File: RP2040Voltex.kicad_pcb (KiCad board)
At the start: 2 copper layers, 180 x 100 mm, 72 parts, among them J2 SWD_Connector, SW1 SW_Push_Dual_x2, SW2 K2-1102SP-C4SC-04, U1 RT8096C, U2 W25Q128JVS, U3 RP2040, U4 PEC16-4015F-N0024, U5 PEC16-4015F-N0024, Y1 Crystal_GND24

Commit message: Make capacitor closer to encoders
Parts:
- moved C18 19.3 mm to (58.8, 80.2), turned to 180 degrees
- moved C21 14.1 mm to (205.1, 80.2), turned to 0 degrees
- moved C20 12.1 mm to (65.3, 80.2), turned to 0 degrees
- moved C19 6.93 mm to (198.5, 80.2), turned to 180 degrees
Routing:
- net VBUS: track 386.8 -> 382.7 mm
- net /GPIO2: track 96.3 -> 99.0 mm
- net /GPIO29_ADC3: track 55.5 -> 58.1 mm
- net /GPIO28_ADC2: track 49.8 -> 52.4 mm
- net /GPIO3: track 90.2 -> 92.5 mm
- net GND: track 60.7 -> 58.8 mm, vias 43 -> 44

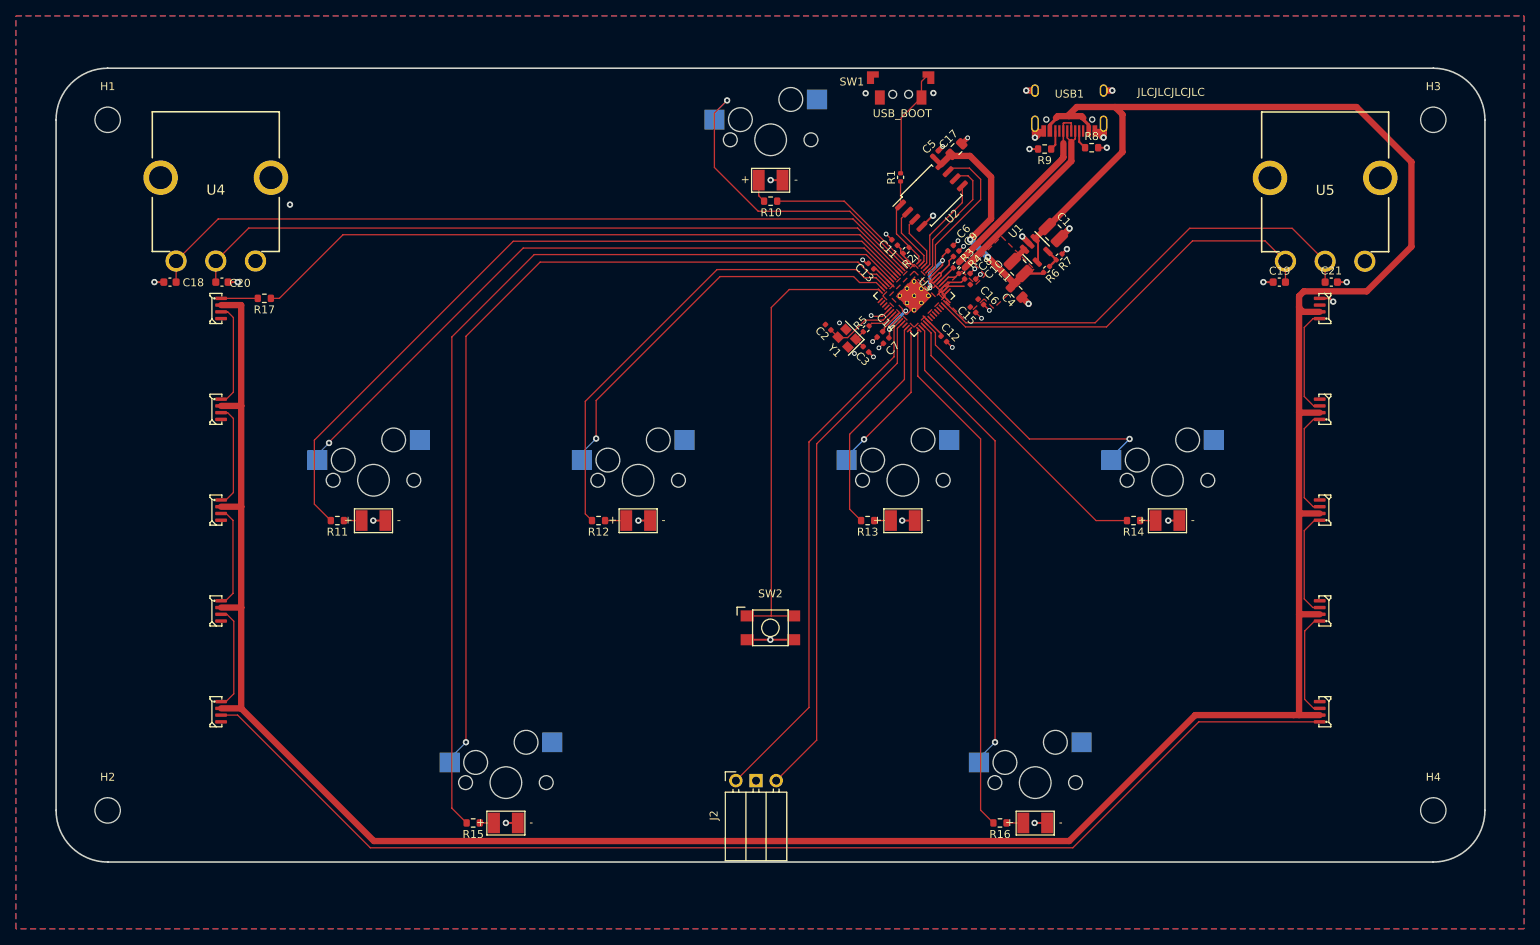
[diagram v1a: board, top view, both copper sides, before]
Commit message: Change front plane to be power plane
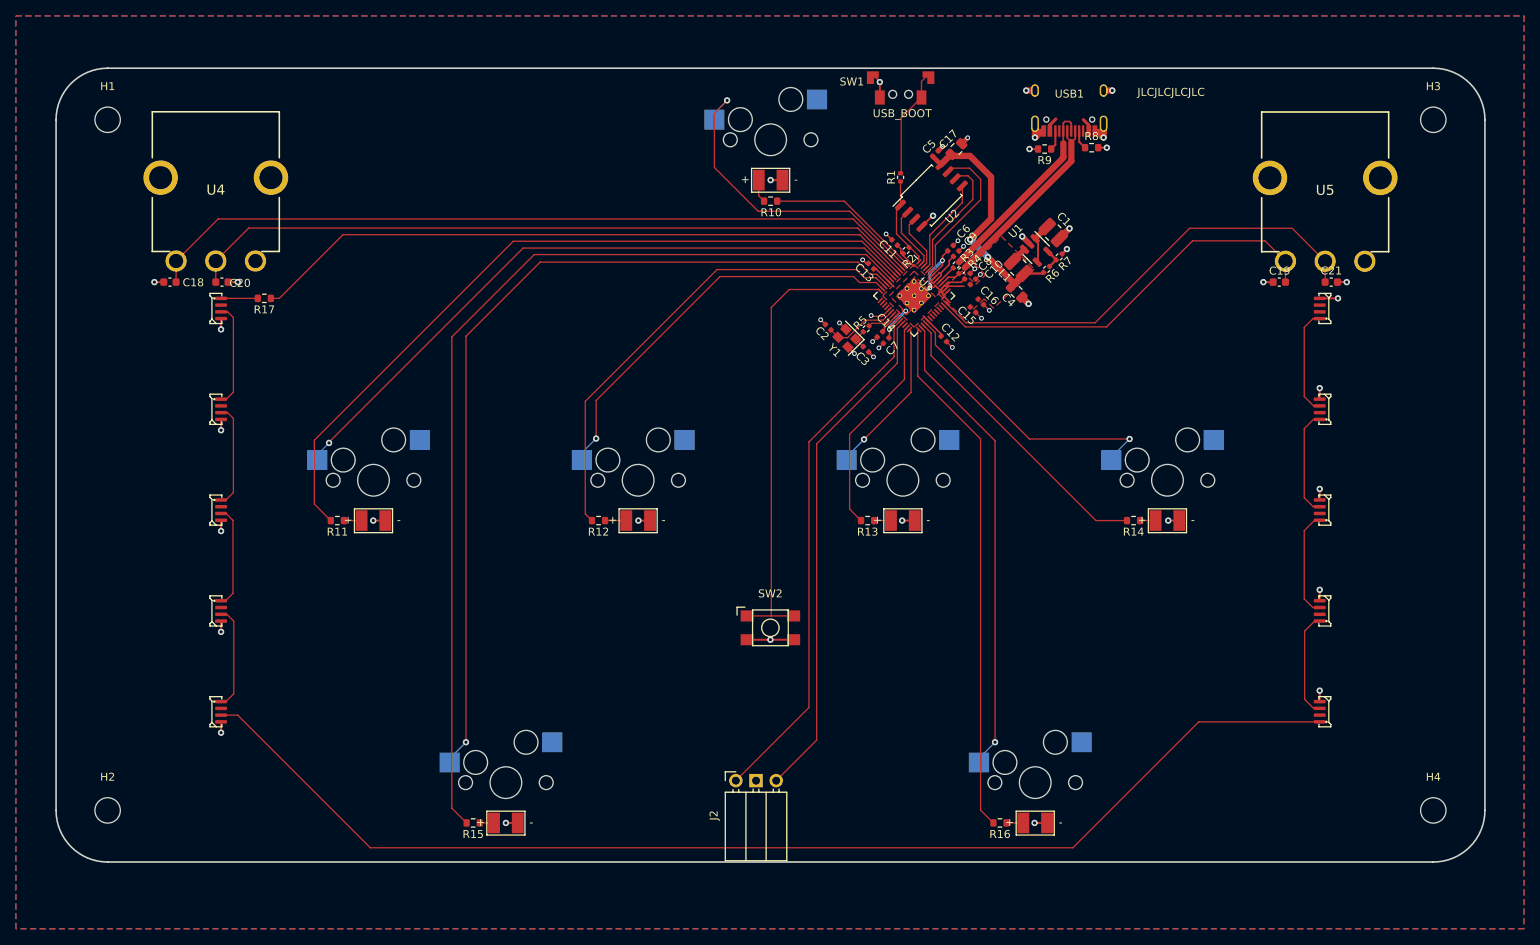
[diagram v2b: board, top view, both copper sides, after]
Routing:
- net VBUS: track 382.7 -> 8.91 mm
- net GND: track 58.8 -> 78.0 mm, vias 44 -> 52
- added copper zone on F.Cu, net VBUS
- removed copper zone on F.Cu, net GND

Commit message: Split led strips + Put usb boot underneath
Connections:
- D5 pad 3: Net-(D5-Pad3) -> unconnected-(D5-Pad3)
- D6 pad 1: Net-(D5-Pad3) -> /GPIO27_ADC1
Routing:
- net Net-(D5-Pad3): track 151.9 -> 0.00 mm
- net /GPIO27_ADC1: track 0.00 -> 94.4 mm
- net unconnected-(D5-Pad3): track 0.00 -> 2.09 mm
- net /~{USB_BOOT}: vias 0 -> 2
